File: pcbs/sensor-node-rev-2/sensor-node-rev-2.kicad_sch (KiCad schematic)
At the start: 81 parts, among them IC1 NPP-301A-700AT, IC2 STM32U031K8U6, J2 DEBUG_CONN, J3 SMA EDGE CONN, J4 UART_CONN, J5 USER_CAP, SW1 SW_Push, U1 STM32U031R8T6, U2 nRF24L01P, U3 INA333xxDGK In-Amp, U4 TLV9001IDCK, X1 16MHz

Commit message: Use new microcontroller package and remove some jumpers
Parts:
- removed C1, C5, C6, C8: 100n, Capacitor_SMD:C_0603_1608Metric, symbol Device:C
- removed C11, C19, C20, C21: EEE-FP0J102AL, libtpms:EEETC1V470P, symbol libtpms:EEE-FP0J102AL
- removed IC2: STM32U031K8U6, libtpms:QFN50P500X500X60-33N-D, symbol libtpms:STM32U031K8U6
- removed JP1: BOOT0 SEL, Connector_PinHeader_2.54mm:PinHeader_1x03_P2.54mm_Vertical, symbol Jumper:Jumper_3_Bridged12
- removed S1: 206-124, libtpms:206124, symbol libtpms:206-124
- removed S2: AYZ0102AGRLC, libtpms:AYZ0102AGRLC, symbol libtpms:AYZ0102AGRLC
- removed SW1: SW_Push, Button_Switch_SMD:SW_SPST_Omron_B3FS-100xP, symbol Switch:SW_Push
- removed U1: STM32U031R8T6, libtpms:LQFP64_STM, symbol libtpms:STM32U031R8T6
- removed U3: INA333xxDGK In-Amp, Package_SO:VSSOP-8_3.0x3.0mm_P0.65mm, symbol Amplifier_Instrumentation:INA333xxDGK
- removed X1: 16MHz, libtpms:830064296, symbol Device:Crystal
- added C1, C5, C6, C8: C_Polarized, libtpms:CAPPM7362X375N, symbol Device:C_Polarized
- added C22: 100n, Capacitor_SMD:C_0402_1005Metric, symbol Device:C
- added IC2: AD8226ARMZ, libtpms:SOP65P490X110-8N, symbol libtpms:AD8226ARMZ
- added JP2: BOOT_SEL, Jumper:SolderJumper-3_P1.3mm_Open_RoundedPad1.0x1.5mm, symbol Jumper:SolderJumper_3_Open
- added S1, S3, S5: CAS-120A1, libtpms:CAS120A1, symbol libtpms:CAS-120A1
- added S4: Pushbutton switch, libtpms:TS2134035BK160SMTTR, symbol libtpms:TS21-34-035-BK-160-SMT-TR
- added U1: STM32U031K8U6, libtpms:QFN50P500X500X60-33N-D, symbol libtpms:STM32U031K8U6
- added Y1: Crystal_16MHz, libtpms:830064296, symbol Device:Crystal_GND24
- C2, C23, C24, C3, C4, C7: footprint Capacitor_SMD:C_0603_1608Metric -> Capacitor_SMD:C_0402_1005Metric
- D1, D2: footprint LED_SMD:LED_0603_1608Metric -> LED_SMD:LED_0402_1005Metric
- R1, R10, R11, R13, R14, R2, R3, R4, R5, R6, R7: footprint Resistor_SMD:R_0603_1608Metric -> Resistor_SMD:R_0402_1005Metric
- renumbered L2 to L1, L1 to L2
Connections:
- net +3.3V: now also S5.3 (NC)
- net BOOT0: now also U1.31 (PF3-BOOT0)
- net GND: now also U2.21 (EPAD), C1.2, C22.2, C5.2, C6.2, C8.2, IC2.5 (-VS), JP2.3 (B), S1.3 (NC), S3.3 (NC), S4.3 (NO_1), S4.4 (NO_2), S4.MP1, S4.MP2, U1.16 (VSS), U1.32 (VSS), U1.33 (EPAD), Y1.2, Y1.4
- net NRF_CE: now also U1.30 (PB7)
- net NRF_CSN: now also U1.29 (PB6)
- net NRF_IRQ: now also U1.25 (PA15)
- net NRF_MISO: now also U1.27 (PB4)
- net NRF_MOSI: now also U1.28 (PB5)
- net NRF_SCK: now also U1.26 (PB3)
- net NRST: now also C22.1, S4.1 (COM_1), S4.2 (COM_2), U1.4 (PF2-NRST)
- net P2110B_DOUT: now also U1.12 (PA6)
- net P2110B_DSET: now also U1.19 (PA9)
- net P2110B_INT: now also U1.20 (PA10)
- net P2110B_RESET: now also U1.18 (PA8)
- net P2110B_VOUT: now also S5.1 (NO)
- net POWER_LED_EN: now also S1.2 (COM)
- net PSENSE_MINUS: now also IC2.4 (+IN), U1.9 (PA3)
- net PSENSE_OUT: now also IC2.7 (VOUT), U1.6 (PA0-CK_IN)
- net PSENSE_PLUS: now also IC2.1 (-IN), U1.10 (PA4)
- net PSENSE_VREF: now also IC2.6 (REF), U1.7 (PA1)
- net SWCLK: now also U1.24 (PA14)
- net SWDIO: now also U1.23 (PA13)
- net USART1_RX: now also U1.13 (PA7)
- net USART1_TX: now also U1.11 (PA5)
- net USER_LED: now also U1.22 (PA12[PA10])
- net USER_LED_EN: now also S3.2 (COM)
- net VDD: now also IC2.8 (+VS), JP2.1 (A), S5.2 (COM), U1.1 (VDD), U1.17 (VDD), U1.5 (VDDA/VREF+)
- net at JP11.1 (A): now also C1.1, C5.1, C6.1, C8.1
- net at R13.2: now also IC2.2 (RG_1)
- net at R13.1: now also IC2.3 (RG_2)
- net NRF_ANT: now reaches AE1.1 (A), C15.2, C16.1
- net at C12.1, U2.10 (XC1): now also Y1.3
- net at C10.1, U2.9 (XC2): now also Y1.1
- net at R1.2: now also JP2.2 (C)
- no-connect marks 52 -> 14
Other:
- note added: "Configuration switches"
- note removed: "Configuration switch"
- moved on the sheet: C2, C23, C24, C3, C4, C7, D1, D2, J2, J4, J5, JP11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

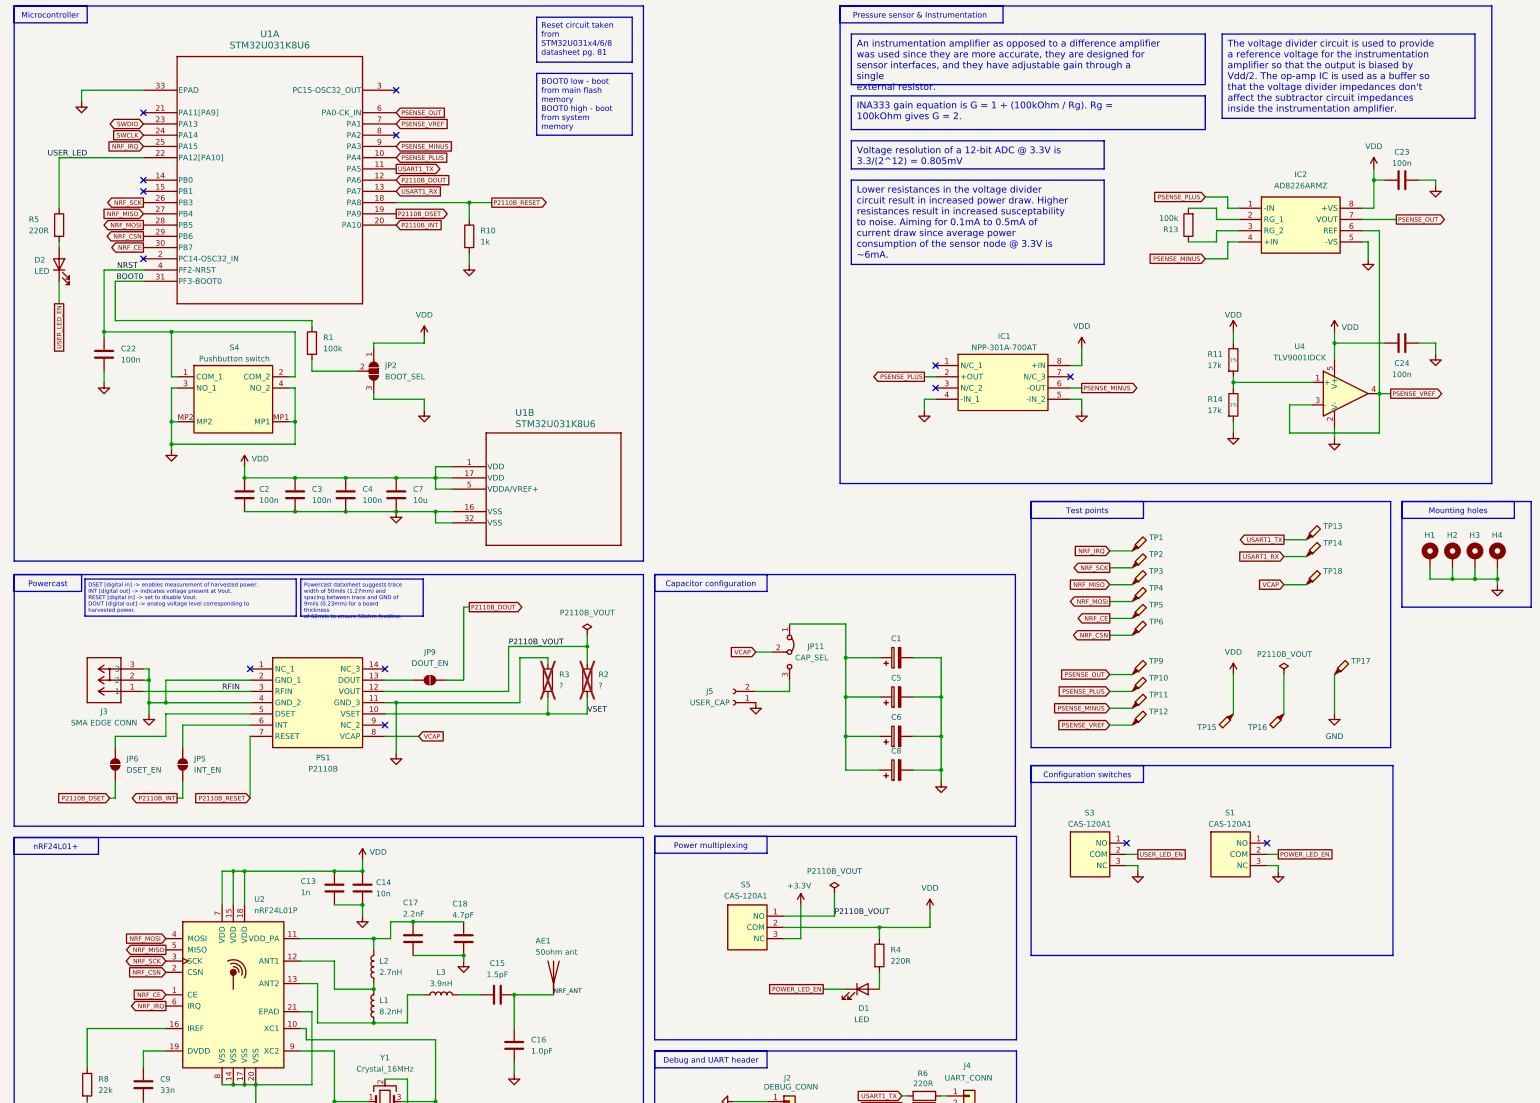
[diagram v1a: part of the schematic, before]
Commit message: Finish routing and layout for sensor node rev 2
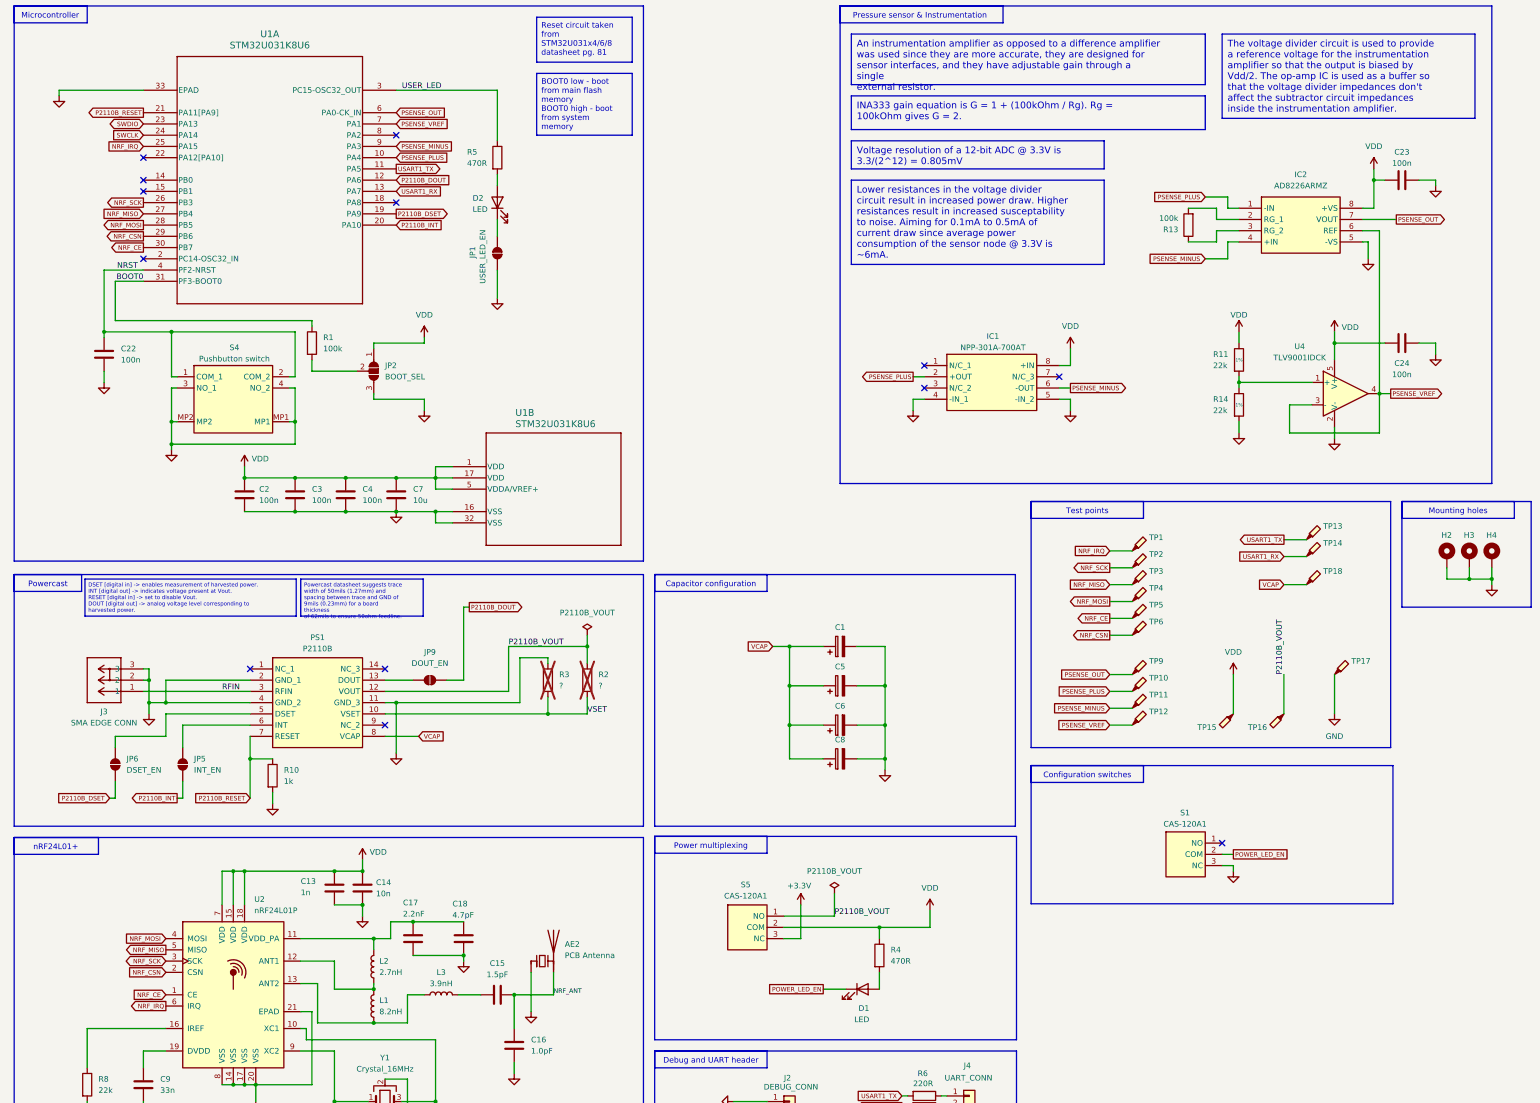
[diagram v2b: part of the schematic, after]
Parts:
- removed AE1: 50ohm ant, symbol Device:Antenna
- removed H1: MountingHole, MountingHole:MountingHole_2.2mm_M2_Pad, symbol Mechanical:MountingHole_Pad
- removed J5: USER_CAP, Connector_PinSocket_2.54mm:PinSocket_1x02_P2.54mm_Vertical, symbol Connector:Conn_01x02_Socket
- removed JP11: CAP_SEL, Connector_PinHeader_2.54mm:PinHeader_1x03_P2.54mm_Vertical, symbol Jumper:Jumper_3_Bridged12
- removed S3: CAS-120A1, libtpms:CAS120A1, symbol libtpms:CAS-120A1
- added AE2: PCB Antenna, libtpms:TI_2G4_Inv_F_Antenna_1, symbol Device:Antenna_Chip
- added JP1: USER_LED_EN, Jumper:SolderJumper-2_P1.3mm_Open_RoundedPad1.0x1.5mm, symbol Jumper:SolderJumper_2_Open
- C1, C5, C6, C8: Manufacturer_Part_Number (none) -> F720J108MMCAQ2; Mouser Part Number (none) -> 581-F720J108MMCAQ2
- C10, C12: Manufacturer_Part_Number 06033C104JAZ2A -> 0402ZA120JAT2A; Mouser Part Number 581-06033C104JAZ2A -> 581-0402ZA120JAT2A
- C13: Manufacturer_Part_Number 06033C104JAZ2A -> 04026C102JAT2A; Mouser Part Number 581-06033C104JAZ2A -> 581-04026C102JAT2A
- C14: Manufacturer_Part_Number 06033C104JAZ2A -> 0402ZD103MAT2A; Mouser Part Number 581-06033C104JAZ2A -> 581-0402ZD103MAT2A
- C15: Manufacturer_Part_Number 06033C104JAZ2A -> VJ0402A1R5BXQPW1BC; Mouser Part Number 581-06033C104JAZ2A -> 77-VJ0402A1R5BXQPBC
- C16: Manufacturer_Part_Number 06033C104JAZ2A -> VJ0402A1R0BXQPW1BC; Mouser Part Number 581-06033C104JAZ2A -> 77-VJ0402A1R0BXQPBC
- C17: Manufacturer_Part_Number 06033C104JAZ2A -> 0402ZC222KAT2A; Mouser Part Number 581-06033C104JAZ2A -> 581-0402ZC222KAT2A
- C18: Manufacturer_Part_Number 06033C104JAZ2A -> 04026A4R7BAT2A; Mouser Part Number 581-06033C104JAZ2A -> 581-04026A4R7BAT2A
- C2, C22, C23, C24, C3, C4: Manufacturer_Part_Number 06033C104JAZ2A -> 0402X7R104KT7AT; Mouser Part Number 581-06033C104JAZ2A -> 581-0402X7R104KT7AT
- C7: Manufacturer_Part_Number GRM188R60J106KE47J -> GRM155R60J106ME05D; Mouser Part Number 81-GRM188R60J106KE7J -> 81-GRM155R60J106M05D
- C9: Manufacturer_Part_Number 06033C104JAZ2A -> GRM155R61A333MA01J; Mouser Part Number 581-06033C104JAZ2A -> 81-GRM155R61A333MA1J
- D1, D2: Manufacturer_Part_Number 150060GS55040 -> 150040GS73220; Mouser Part Number 710-150060GS55040 -> 710-150040GS73220
- L1: Manufacturer_Part_Number (none) -> LQG15HS8N2H02D; Mouser Part Number (none) -> 81-LQG15HS8N2H02D
- L2: Manufacturer_Part_Number (none) -> LQG15HN2N7C02D; Mouser Part Number (none) -> 81-LQG15HN2N7C02D
- L3: Manufacturer_Part_Number (none) -> LQG15HZ3N9C02D; Mouser Part Number (none) -> 81-LQG15HZ3N9C02D
- R1, R13: Manufacturer_Part_Number ERJ-PA3D1003V -> ERJ-U02J104X; Mouser Part Number 667-ERJ-PA3D1003V -> 667-ERJ-U02J104X
- R10: Manufacturer_Part_Number ERJ-PA3D1003V -> ERJ-2GEJ102X; Mouser Part Number 667-ERJ-PA3D1003V -> 667-ERJ-2GEJ102X
- R11, R14: value 17k -> 22k; Manufacturer_Part_Number ERJ-PA3D1003V -> ERJ-H2RD2202X; Mouser Part Number 667-ERJ-PA3D1003V -> 667-ERJ-H2RD2202X
- R2, R3: Manufacturer_Part_Number CRCW06031M58FKEA -> (none); Mouser Part Number 71-CRCW06031M58FKEA -> (none)
- R4, R5: value 220R -> 470R; Manufacturer_Part_Number ERJ-PA3D2200V -> ERJ-2RHD471X; Mouser Part Number 667-ERJ-PA3D2200V -> 667-ERJ-2RHD471X
- R6, R7: Manufacturer_Part_Number ERJ-PA3D2200V -> ERJ-2RHD2200X; Mouser Part Number 667-ERJ-PA3D2200V -> 667-ERJ-2RHD2200X
- R8: Manufacturer_Part_Number CRCW06031M58FKEA -> ERJ-H2RD2202X; Mouser Part Number 71-CRCW06031M58FKEA -> 667-ERJ-H2RD2202X
- TP1, TP10, TP11, TP12, TP2, TP3, TP4, TP5, TP6, TP9: footprint TestPoint:TestPoint_Pad_2.0x2.0mm -> TestPoint:TestPoint_Pad_1.5x1.5mm
- U1: Manufacturer_Part_Number (none) -> STM32U031K8U6; Mouser Part Number (none) -> 511-STM32U031K8U6
- U2: Manufacturer_Part_Number (none) -> NRF24L01P; Mouser Part Number (none) -> 949-NRF24L01P
- U4: Manufacturer_Part_Number (none) -> TLV9001IDCKR; Mouser Part Number (none) -> 595-TLV9001IDCKR
- Y1: Manufacturer_Part_Number (none) -> 830064296; Mouser Part Number (none) -> 710-830064296
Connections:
- net GND: now also AE2.1 (FEED), JP1.1 (A)
- net NRF_ANT: now also AE2.2 (PCB_Trace)
- net P2110B_RESET: now also U1.21 (PA11[PA9]); no longer U1.18 (PA8)
- net P2110B_VOUT: now also TP16.1
- net USER_LED: now also U1.3 (PC15-OSC32_OUT); no longer U1.22 (PA12[PA10])
- net VCAP: now also C1.1, C5.1, C6.1, C8.1
- net USER_LED_EN: no longer names the net of D2.1 (K)
- net USER_LED_EN: now also JP1.2 (B)
- no-connect marks 14 -> 13
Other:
- moved on the sheet: C1, C5, C6, C8, D2, H2, H3, H4, IC1, R10, R11, R14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
